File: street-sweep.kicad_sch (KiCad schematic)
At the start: 56 parts, among them J1 PJ-320A, P1 GT-USB-7010ASV, SW10 SW_Push, SW10_r1 SW_Push, SW11 SW_Push, SW11_r1 SW_Push, SW12 SW_Push, SW12_r1 SW_Push, SW13_r1 SW_Push, SW14 SW_Push, SW14_r1 SW_Push, SW15 SW_Push, SW15_r1 SW_Push, SW16 SW_Push, SW16_r1 SW_Push, SW17 SW_Push, SW17_r1 SW_Push, SW18 SW_Push, SW18_r1 SW_Push, SW2 SW_Push, SW20 SW_Push, SW21 SW_Push, SW2_r1 SW_Push, SW3 SW_Push, SW3_r1 SW_Push, SW4 SW_Push, SW4_r1 SW_Push, SW5 SW_Push, SW5_r1 SW_Push, SW6 SW_Push, SW6_r1 SW_Push, SW7_r1 SW_Push, SW8 SW_Push, SW8_r1 SW_Push, SW9 SW_Push, SW9_r1 SW_Push, U1 CH552G

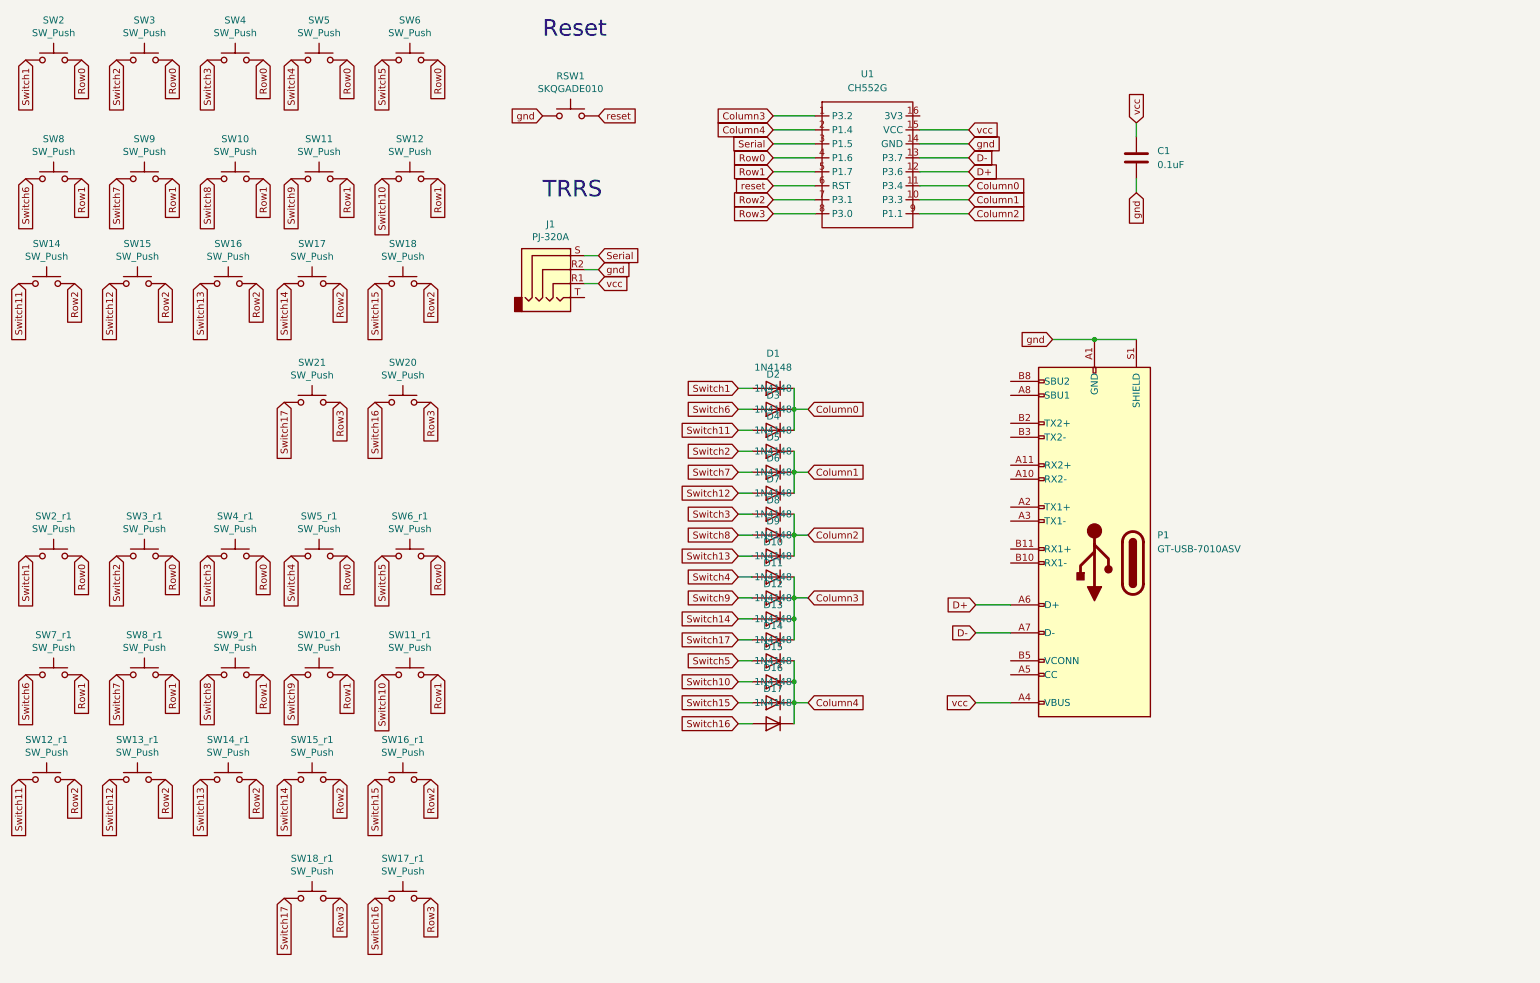
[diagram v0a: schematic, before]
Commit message: Made first pass at converting to an STM32 based design.
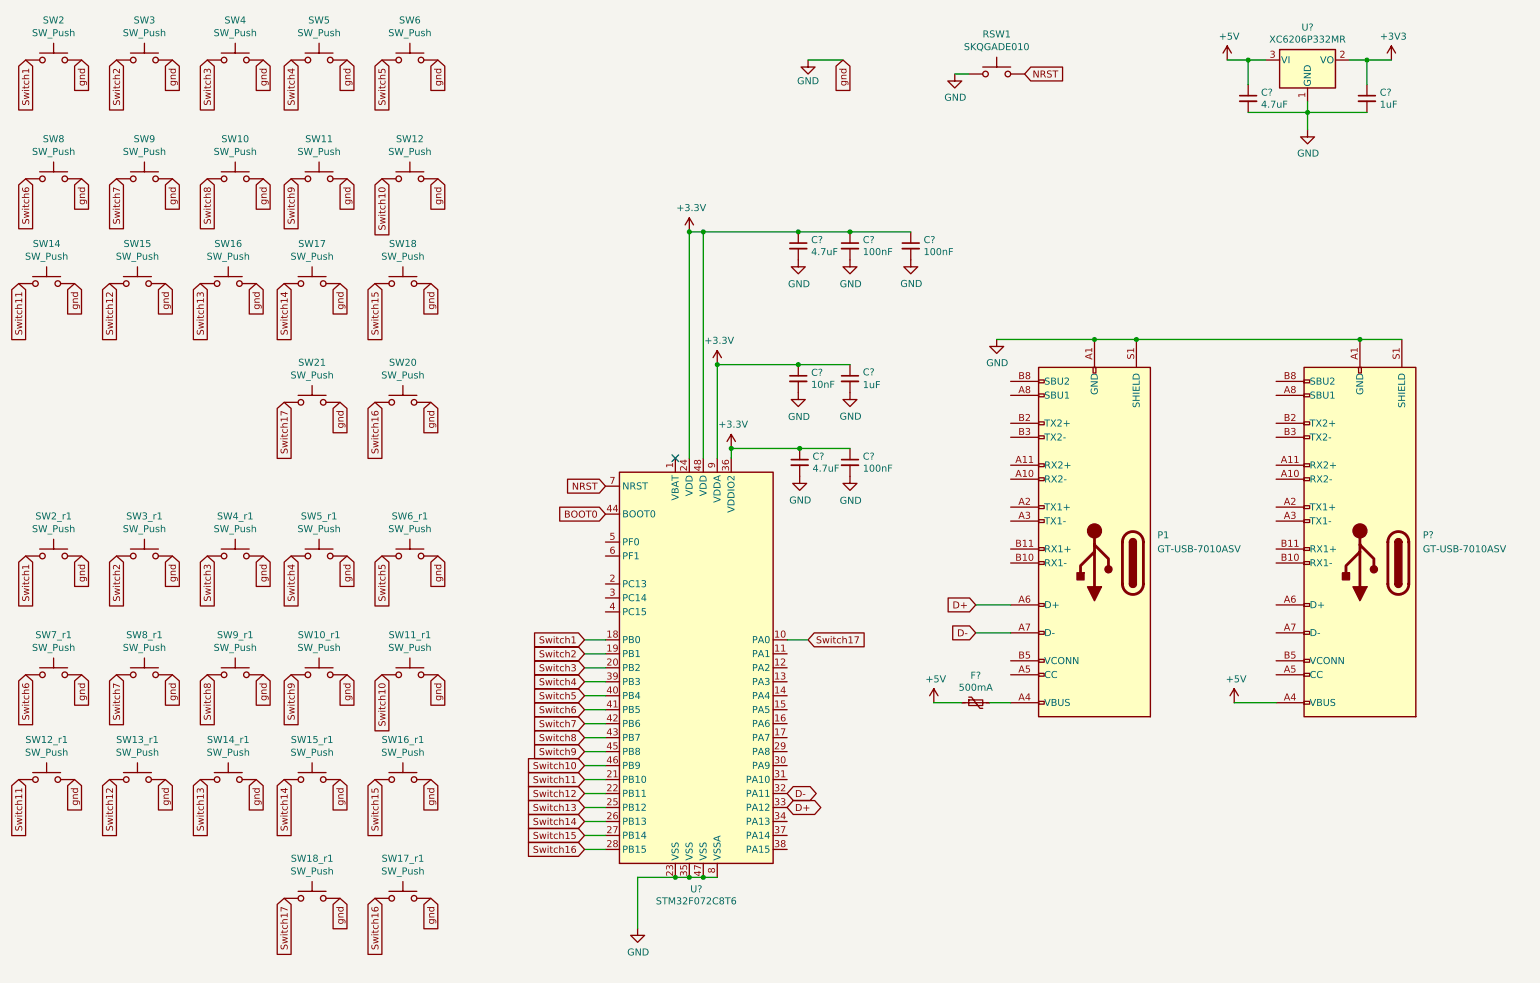
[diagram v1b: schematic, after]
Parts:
- removed C1: 0.1uF, Capacitor_SMD:C_0805_2012Metric_Pad1.18x1.45mm_HandSolder, symbol Device:C
- removed D1, D10, D11, D12, D13, D14, D15, D16, D17, D2, D3, D4, D5, D6, D7, D8, D9: 1N4148, Diode_SMD:D_SOD-123, symbol Diode:1N4148
- removed J1: PJ-320A, Connector_Audio:Jack_3.5mm_PJ320D_Horizontal, symbol Connector:AudioJack4
- removed U1: CH552G, CH552G:CH552G, symbol CH552G:CH552G
- added C? (x3): 4.7uF, Capacitor_SMD:C_0603_1608Metric_Pad1.05x0.95mm_HandSolder, symbol Device:C_Small
- added C? (x2): 1uF, Capacitor_SMD:C_0603_1608Metric_Pad1.05x0.95mm_HandSolder, symbol Device:C_Small
- added C? (x3): 100nF, Capacitor_SMD:C_0603_1608Metric_Pad1.05x0.95mm_HandSolder, symbol Device:C_Small
- added C?: 10nF, Capacitor_SMD:C_0603_1608Metric_Pad1.05x0.95mm_HandSolder, symbol Device:C_Small
- added F?: 500mA, Capacitor_SMD:C_1206_3216Metric_Pad1.42x1.75mm_HandSolder, symbol Device:Polyfuse_Small
- added P?: GT-USB-7010ASV, Connector_USB:USB_C_Receptacle_G-Switch_GT-USB-7010ASV, symbol Connector:USB_C_Plug
- added U?: STM32F072C8T6, Package_QFP:LQFP-48_7x7mm_P0.5mm, symbol MCU_ST_STM32F0:STM32F072C8Tx
- added U?: XC6206P332MR, Package_TO_SOT_SMD:SOT-23-3, symbol Regulator_Linear:XC6206PxxxMR
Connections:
- net Row1 is gone; now on net GND: SW10.2, SW10_r1.2, SW11.2, SW11_r1.2, SW12.2, SW7_r1.2, SW8.2, SW8_r1.2, SW9.2, SW9_r1.2
- net Row2 is gone; now on net GND: SW12_r1.2, SW13_r1.2, SW14.2, SW14_r1.2, SW15.2, SW15_r1.2, SW16.2, SW16_r1.2, SW17.2, SW18.2
- net Row3 is gone; now on net GND: SW17_r1.2, SW18_r1.2, SW20.2, SW21.2
- net gnd is gone; now on net GND: P1.A1 (GND), P1.A12 (GND), P1.B1 (GND), P1.B12 (GND), P1.S1 (SHIELD), RSW1.1
- net D+: now also U?.33 (PA12)
- net D-: now also U?.32 (PA11)
- net Switch1: now also U?.18 (PB0)
- net Switch10: now also U?.46 (PB9)
- net Switch11: now also U?.21 (PB10)
- net Switch12: now also U?.22 (PB11)
- net Switch13: now also U?.25 (PB12)
- net Switch14: now also U?.26 (PB13)
- net Switch15: now also U?.27 (PB14)
- net Switch16: now also U?.28 (PB15)
- net Switch17: now also U?.10 (PA0)
- net Switch2: now also U?.19 (PB1)
- net Switch3: now also U?.20 (PB2)
- net Switch4: now also U?.39 (PB3)
- net Switch5: now also U?.40 (PB4)
- net Switch6: now also U?.41 (PB5)
- net Switch7: now also U?.42 (PB6)
- net Switch8: now also U?.43 (PB7)
- net Switch9: now also U?.45 (PB8)
- net Row0 renamed GND
- net GND: now also C?.2, C?.2, C?.2, C?.2, C?.2, C?.2, C?.2, C?.2, C?.2, P?.A1 (GND), P?.A12 (GND), P?.B1 (GND), P?.B12 (GND), P?.S1 (SHIELD), U?.1 (GND), U?.23 (VSS), U?.35 (VSS), U?.47 (VSS), U?.8 (VSSA)
- net reset renamed NRST
- net NRST: now also U?.7 (NRST)
- net vcc: no longer names the net of P1.A4 (VBUS), P1.A9 (VBUS), P1.B4 (VBUS), P1.B9 (VBUS)
- net vcc: now also F?.2
- new net +3.3V: C?.1, C?.1, C?.1, C?.1, C?.1, C?.1, C?.1, U?.24 (VDD), U?.36 (VDDIO2), U?.48 (VDD), U?.9 (VDDA)
- new net +3V3: C?.1, U?.2 (VO)
- new net +5V: C?.1, F?.1, P?.A4 (VBUS), P?.A9 (VBUS), P?.B4 (VBUS), P?.B9 (VBUS), U?.3 (VI)
- new net BOOT0: U?.44 (BOOT0)
- no-connect marks 0 -> 1
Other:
- note removed: "Reset"
- note removed: "TRRS"
- moved on the sheet: RSW1

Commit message: Latest changes on STM32
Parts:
- removed C? (x3): 100nF, Capacitor_SMD:C_0603_1608Metric_Pad1.05x0.95mm_HandSolder, symbol Device:C_Small
- removed C?: 10nF, Capacitor_SMD:C_0603_1608Metric_Pad1.05x0.95mm_HandSolder, symbol Device:C_Small
- removed F?: 500mA, Capacitor_SMD:C_1206_3216Metric_Pad1.42x1.75mm_HandSolder, symbol Device:Polyfuse_Small
- added R1, R2: 5.1k, Resistor_SMD:R_0805_2012Metric, symbol Device:R_Small
- added SW1: RotaryEncoder_Switch, Rotary_Encoder:RotaryEncoder_Alps_EC11E-Switch_Vertical_H20mm, symbol Device:RotaryEncoder_Switch
- C1, C2, C3, C4, C5: renamed from C?; footprint Capacitor_SMD:C_0603_1608Metric_Pad1.05x0.95mm_HandSolder -> Capacitor_SMD:C_0805_2012Metric
- RSW1: footprint Button_Switch_SMD:SW_SPST_SKQG_WithoutStem -> Connector_PinHeader_2.54mm:PinHeader_1x02_P2.54mm_Vertical
- gave numbers to parts that had none: 3
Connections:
- net +5V: now also P1.A4 (VBUS), P1.A9 (VBUS), P1.B4 (VBUS), P1.B9 (VBUS)
- net GND: now also R1.1, R2.1, SW1.C, SW1.S1
- net Switch18: now reaches U1.11 (PA1)
- net Switch18: now also SW1.S2
- net Enc_A: now reaches U1.12 (PA2)
- net Enc_A: now also SW1.A
- net Enc_B: now reaches U1.13 (PA3)
- net Enc_B: now also SW1.B
- net Serial D+: now reaches U1.30 (PA9)
- net Serial D+: now also P2.A6 (D+)
- net Serial D-: now reaches U1.31 (PA10)
- net Serial D-: now also P2.A7 (D-)
- net at P1.A5 (CC): now also R2.2
- net at P1.B5 (VCONN): now also R1.2
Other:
- moved on the sheet: C2, C3
